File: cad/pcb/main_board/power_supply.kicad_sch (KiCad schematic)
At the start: 14 parts, among them SW2 SW_DIP_x01, U2 TLV75533PDRVR

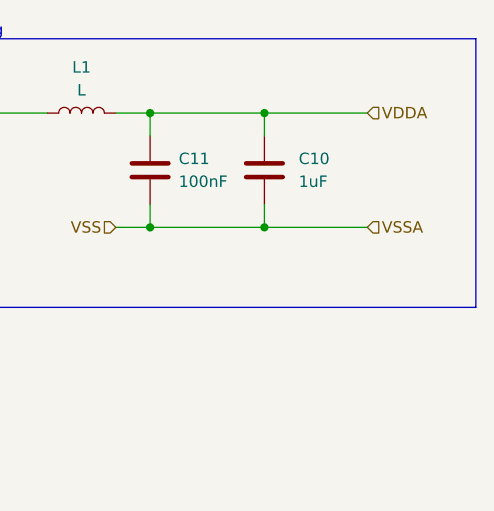
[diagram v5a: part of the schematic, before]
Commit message: Hooking up ThermoCouple pins first layout of TCs
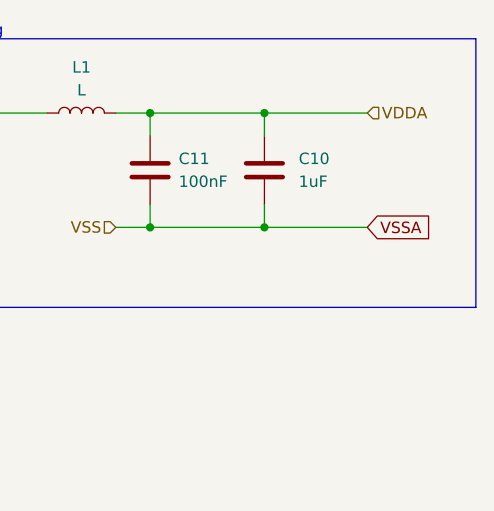
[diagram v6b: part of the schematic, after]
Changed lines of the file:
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@@
+		)
+	)
+	(global_label "VSSA"
+		(shape input)
+		(at 214.63 72.39 0)
+		(fields_autoplaced yes)
+		(effects
+			(font
+				(size 1.27 1.27)
+			)
+			(justify left)
+		)
+		(property "Intersheetrefs" "${INTERSHEET_REFS}"
+			(at 222.2114 72.39 0)
+			(effects
+				(font
+					(size 1.27 1.27)
+				)
+				(justify left)
+				(hide yes)
+			)
 		)
 	)
@@
 		)
 	)
-	(hierarchical_label "VSSA"
-		(shape input)
-		(at 214.63 72.39 0)
-		(fields_autoplaced yes)
-		(effects
-			(font
-				(size 1.27 1.27)
-			)
-			(justify left)
-		)
-	)

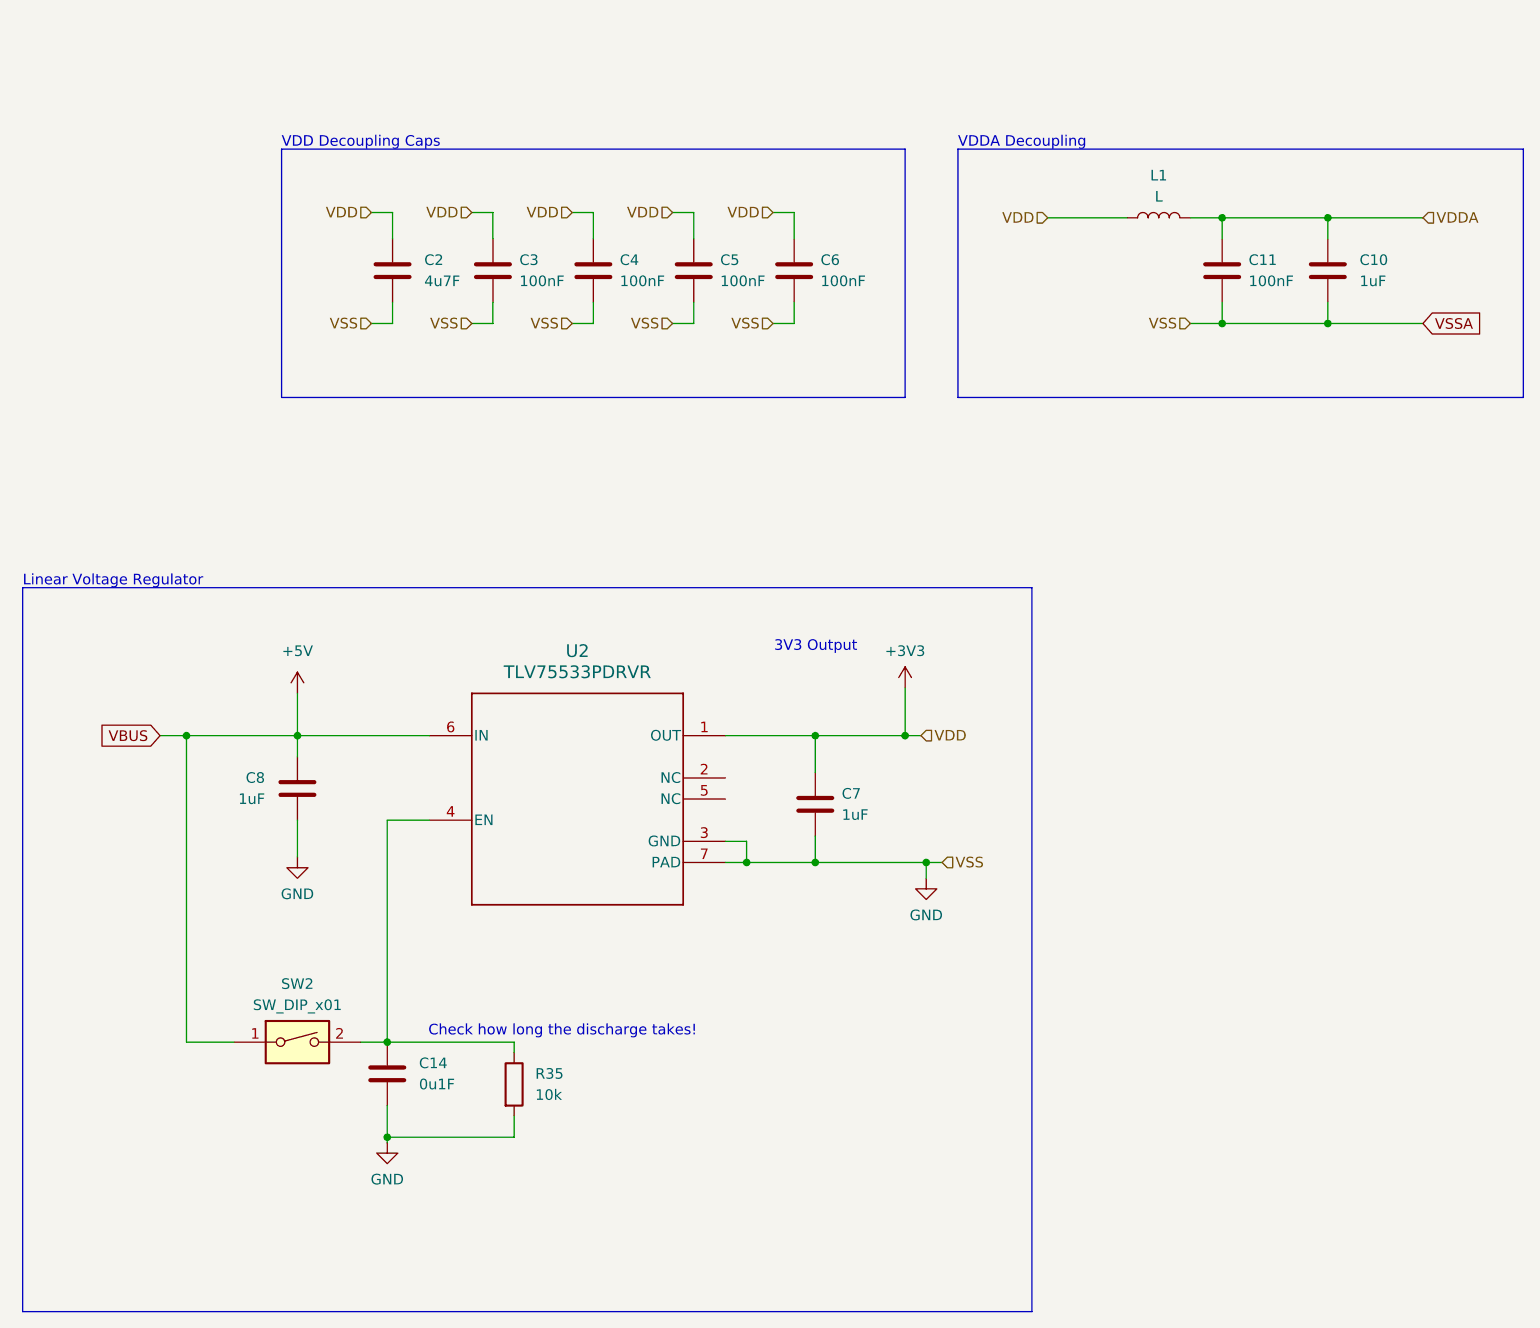
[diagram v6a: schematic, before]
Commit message: Adding JTAG Interface + POGO Pads
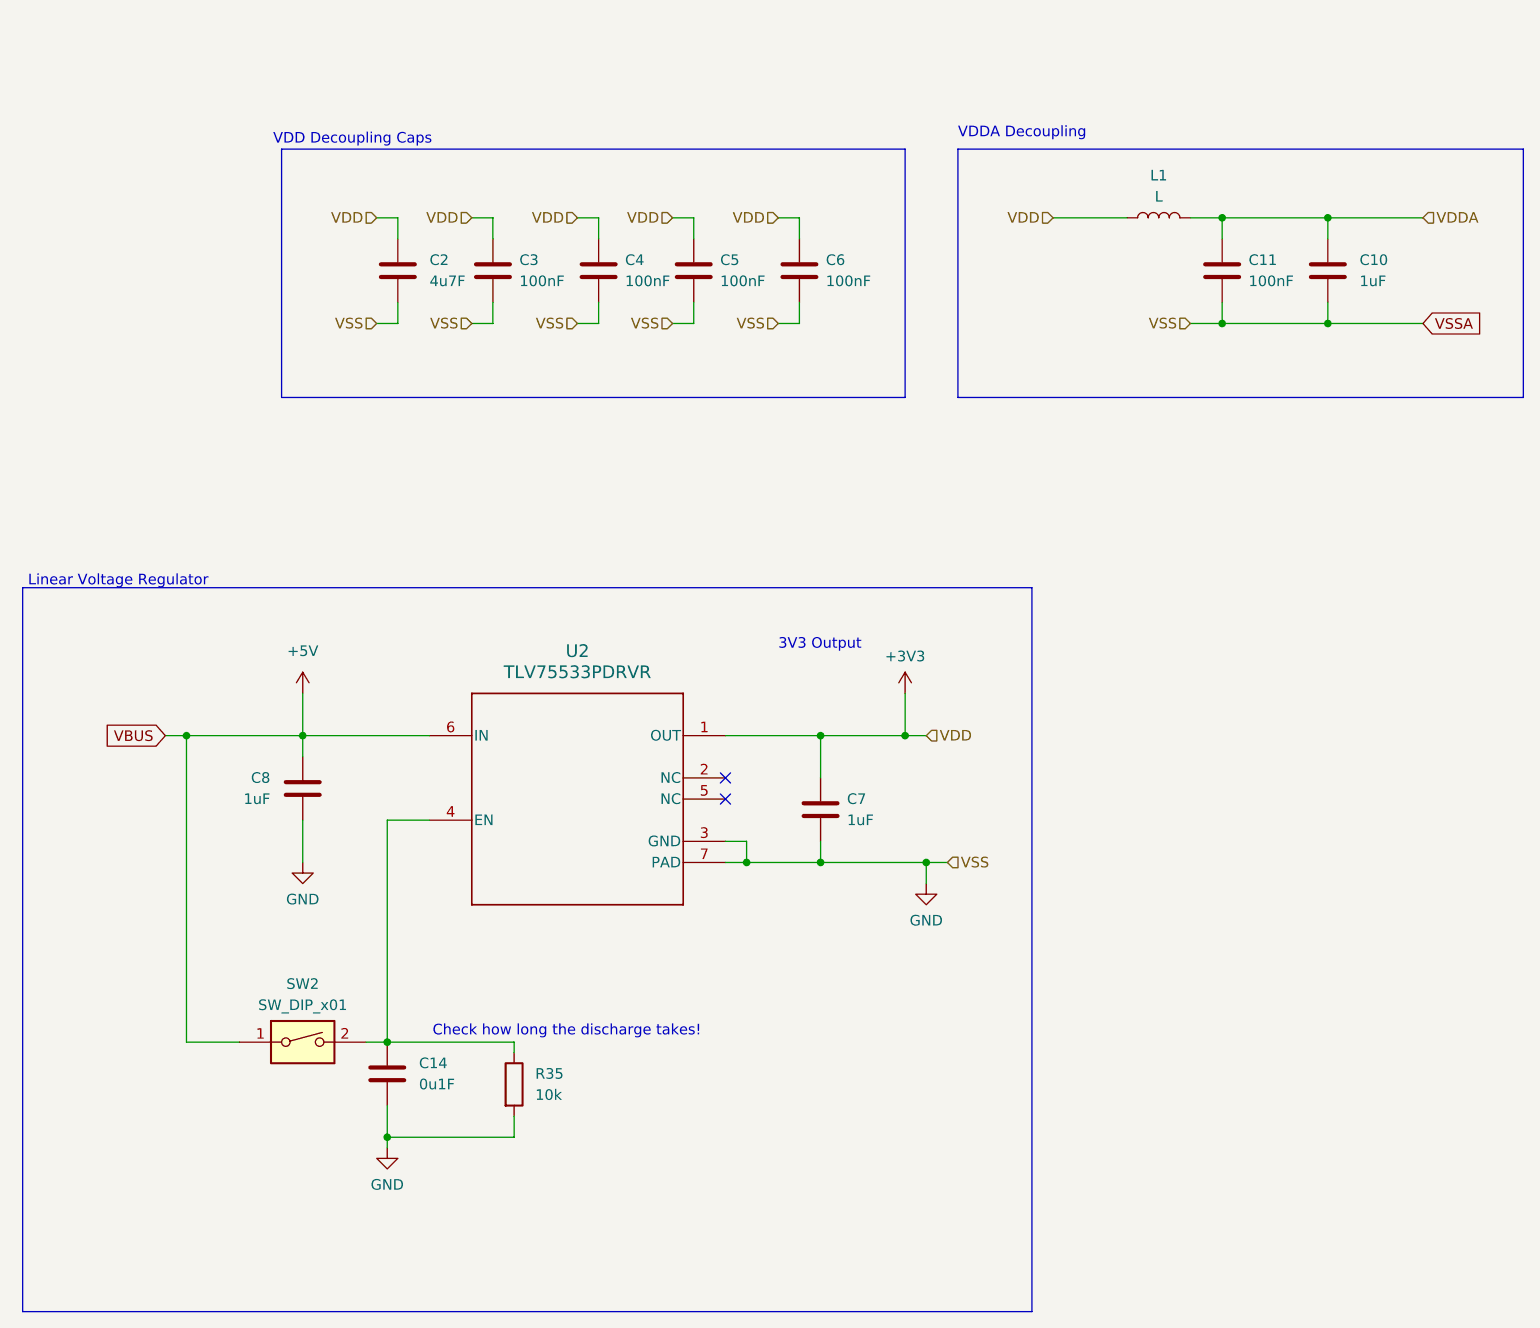
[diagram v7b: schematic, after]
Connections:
- no-connect marks 0 -> 2
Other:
- moved on the sheet: C2, C4, C6, C7, C8, SW2

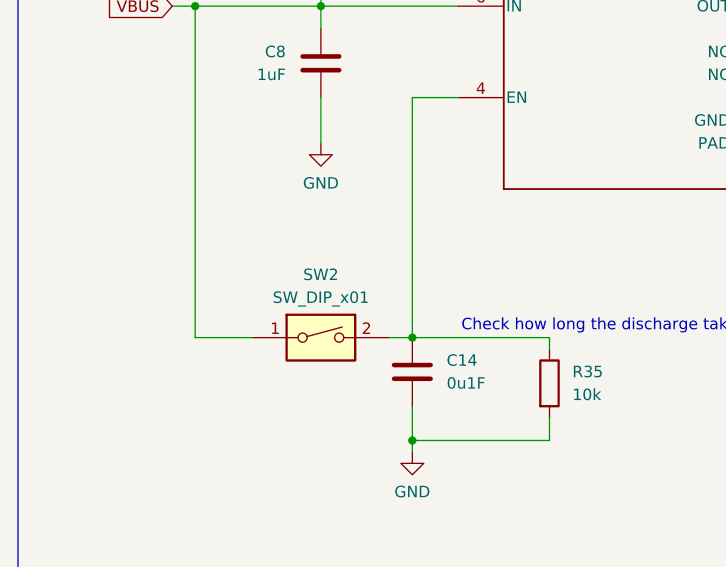
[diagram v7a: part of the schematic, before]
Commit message: More bunching together, some jtag, voltage regulator layout
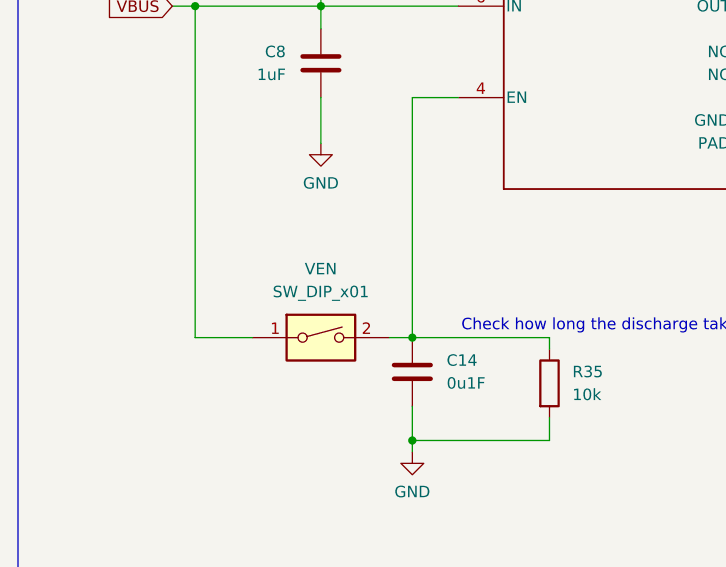
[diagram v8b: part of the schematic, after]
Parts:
- renumbered SW2 to VEN
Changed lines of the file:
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@@
 		(dnp no)
 		(fields_autoplaced yes)
-		(property "Reference" "SW2"
-			(at 80.01 151.765 0)
+		(property "Reference" "VEN"
+			(at 80.01 151.13 0)
 			(effects
 				(font
@@
 		)
 		(property "Value" "SW_DIP_x01"
-			(at 80.01 154.305 0)
+			(at 80.01 153.67 0)
 			(effects
 				(font
@@
 			(project "main_board"
 				(path "/6c1b8035-64fa-4797-a506-5c9583cb241c/89e1b759-e3da-4961-90e8-6f92bf79e795/8c2804c0-90ed-471e-8073-15cf7e3965b7"
-					(reference "SW2")
+					(reference "VEN")
 					(unit 1)
 				)
